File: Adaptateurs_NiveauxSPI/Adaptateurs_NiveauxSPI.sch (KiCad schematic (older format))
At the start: 21 parts, among them P1 CONN_01X07, P2 CONN_01X08, P3 CONN_01X07, P4 CONN_01X12, P5 CONN_01X07, P6 CONN_01X09, P7 CONN_01X07, P8 CONN_01X12, U1 CON_5V_3-3V, U2 CON_5V_3-3V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

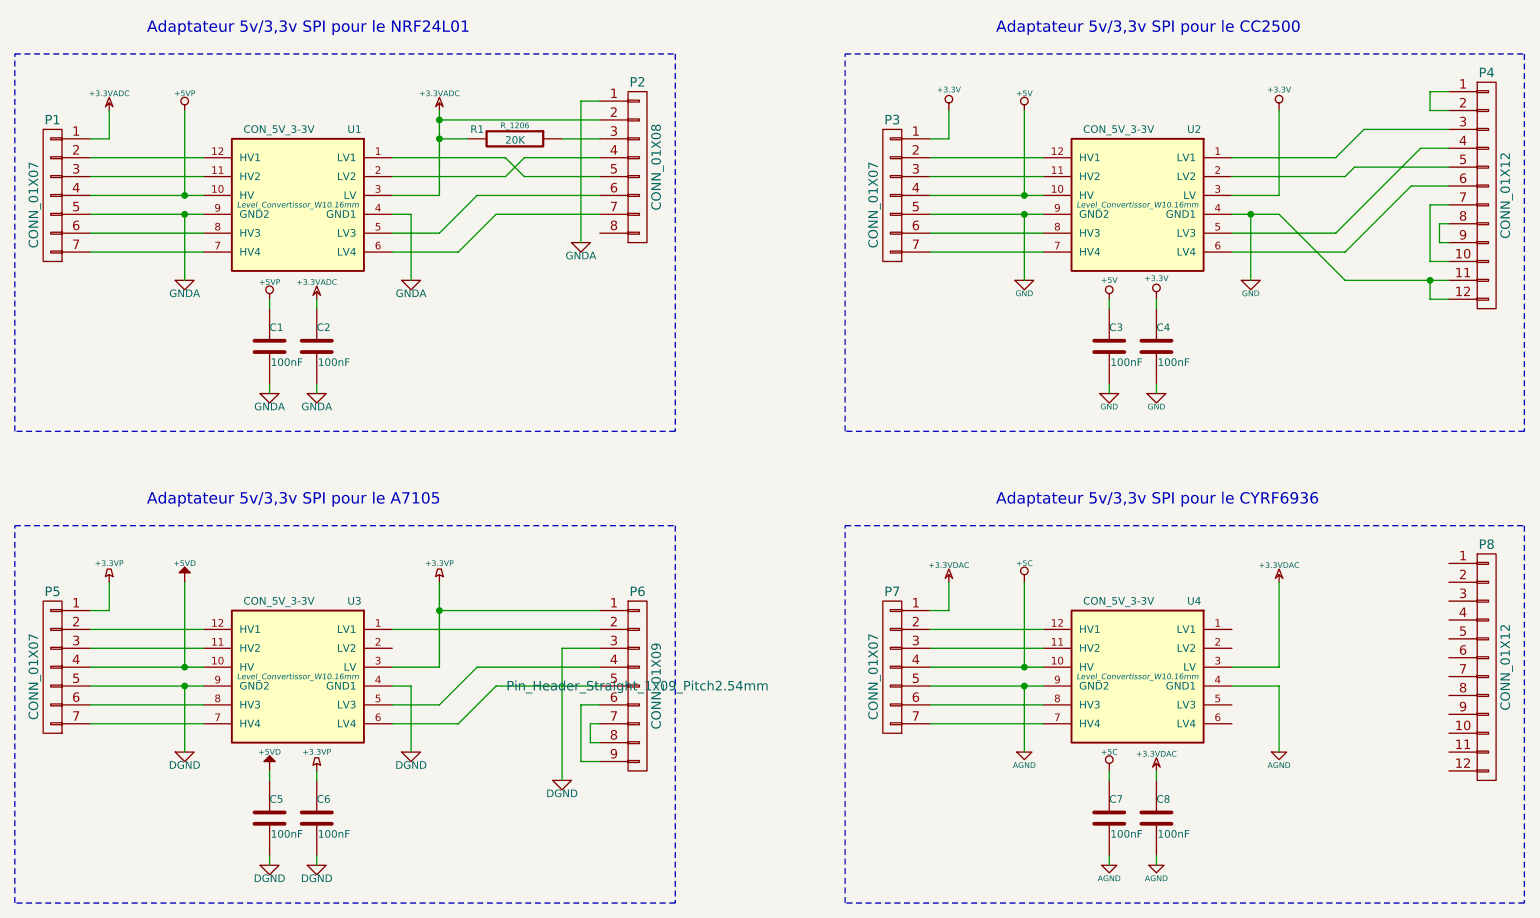
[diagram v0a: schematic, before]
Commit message: Update SPI boards
- Add CYRF9636 board
- Update CC2500 board
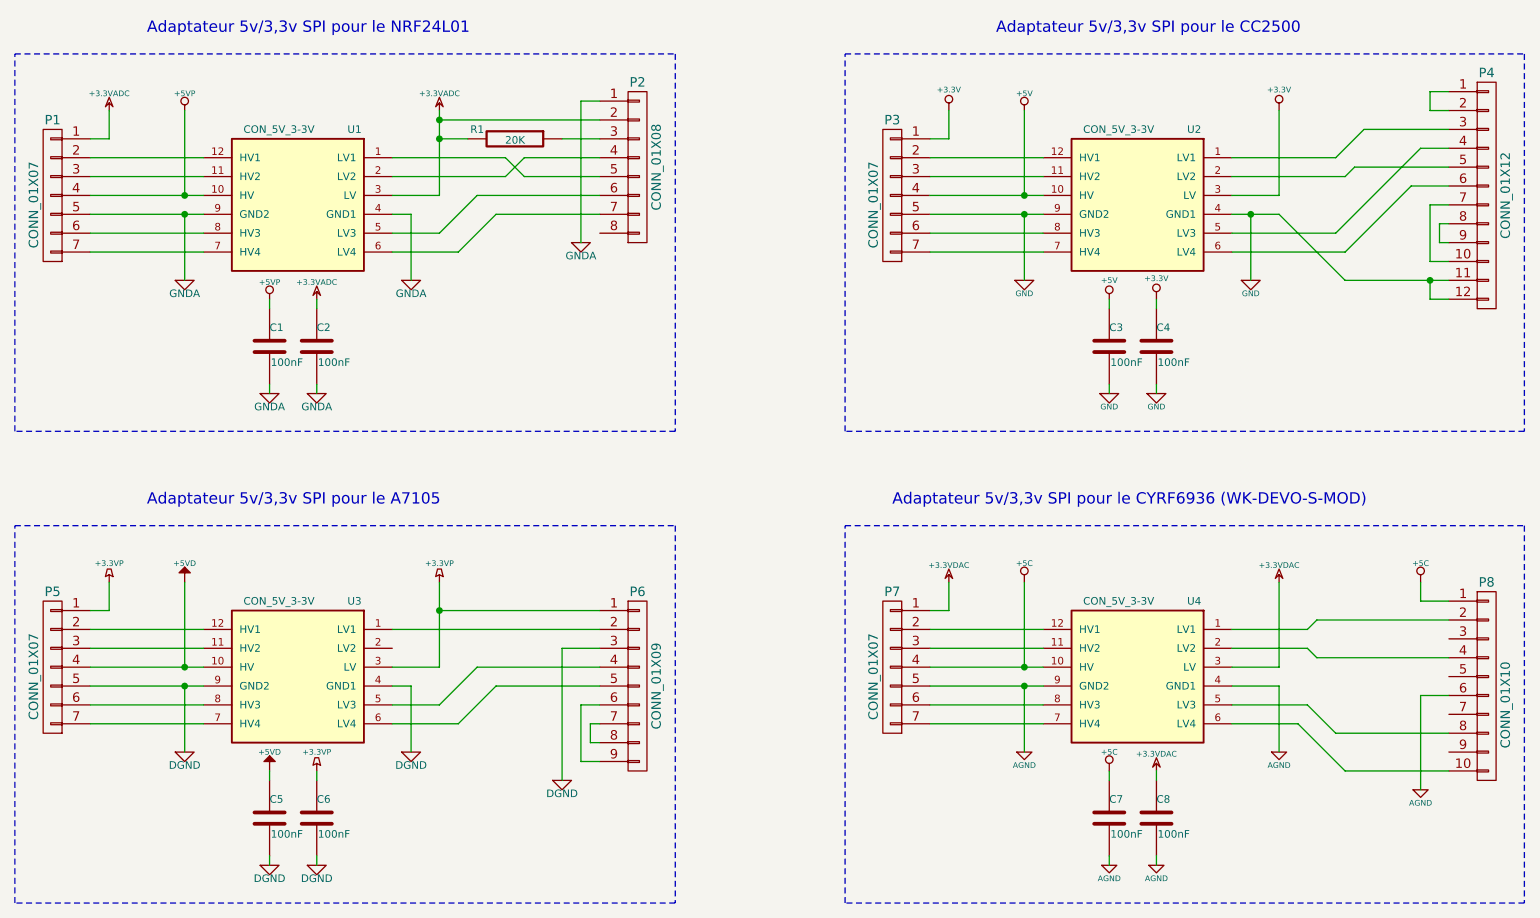
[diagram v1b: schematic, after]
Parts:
- removed P8: CONN_01X12, Pin_Header_Straight_2x06_Pitch2.54mm, symbol CONN_01X12
- added P8: CONN_01X10, Pin_Header_Straight_2x05_Pitch2.54mm, symbol CONN_01X10
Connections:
- net +5C: now also P8.1 (P1)
- net AGND: now also P8.6 (P6)
- net at U4.1 (LV1): now also P8.2 (P2)
- net at U4.2 (LV2): now also P8.4 (P4)
- net at U4.5 (LV3): now also P8.8 (P8)
- net at U4.6 (LV4): now also P8.10 (P10)
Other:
- note added: "Adaptateur 5v/3,3v SPI pour le CYRF6936 (WK-DEVO-S-MOD)"
- note removed: "Adaptateur 5v/3,3v SPI pour le CYRF6936"
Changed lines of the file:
@@
 Sheet 1 1
 Title "Adaptateur Niveaux SPI 5v/3,3v"
-Date "2018-08-24"
+Date "2018-09-07"
 Rev "0.1"
 Comp ""
@@
 F 0 "U1" H 2900 3000 40  0000 C CNN
 F 1 "CON_5V_3-3V" H 3300 3000 40  0000 C CNN
-F 2 "Level_Convertissor_W10.16mm" H 3200 2600 30  0000 C CIN
+F 2 "Level_Convertissor_W10.16mm" H 3200 2600 30  0001 C CIN
 F 3 "" H 3200 2600 60  0001 C CNN
 	1    3200 2600
@@
 F 0 "R1" V 4300 2050 40  0000 C CNN
 F 1 "20K" V 4357 2251 40  0000 C CNN
-F 2 "R_1206" V 4280 2250 30  0000 C CNN
+F 2 "R_1206" V 4280 2250 30  0001 C CNN
 F 3 "" H 4350 2250 30  0000 C CNN
 	1    4350 2250
@@
 F 0 "U2" H 7350 3000 40  0000 C CNN
 F 1 "CON_5V_3-3V" H 7750 3000 40  0000 C CNN
-F 2 "Level_Convertissor_W10.16mm" H 7650 2600 30  0000 C CIN
+F 2 "Level_Convertissor_W10.16mm" H 7650 2600 30  0001 C CIN
 F 3 "" H 7650 2600 60  0001 C CNN
 	1    7650 2600
@@
 F 0 "U3" H 2900 5500 40  0000 C CNN
 F 1 "CON_5V_3-3V" H 3300 5500 40  0000 C CNN
-F 2 "Level_Convertissor_W10.16mm" H 3200 5100 30  0000 C CIN
+F 2 "Level_Convertissor_W10.16mm" H 3200 5100 30  0001 C CIN
 F 3 "" H 3200 5100 60  0001 C CNN
 	1    3200 5100
@@
 F 0 "P6" H 5000 5650 50  0000 C CNN
 F 1 "CONN_01X09" V 5100 5150 50  0000 C CNN
-F 2 "Pin_Header_Straight_1x09_Pitch2.54mm" H 5000 5150 50  0000 C CNN
+F 2 "Pin_Header_Straight_1x09_Pitch2.54mm" H 5000 5150 50  0001 C CNN
 F 3 "" H 5000 5150 50  0000 C CNN
 	1    5000 5150
@@
 Wire Wire Line
 	4700 5250 4800 5250
-$Comp
-L CONN_01X12 P8
-U 1 1 5B812A01
-P 9450 5050
-F 0 "P8" H 9500 5700 50  0000 C CNN
-F 1 "CONN_01X12" V 9600 5050 50  0000 C CNN
-F 2 "Pin_Header_Straight_2x06_Pitch2.54mm" H 9500 4850 50  0001 C CNN
-F 3 "" H 9500 4850 50  0000 C CNN
-	1    9450 5050
-	1    0    0    -1
-$EndComp
 $Comp
 L CONN_01X07 P7
@@
 F 0 "U4" H 7350 5500 40  0000 C CNN
 F 1 "CON_5V_3-3V" H 7750 5500 40  0000 C CNN
-F 2 "Level_Convertissor_W10.16mm" H 7650 5100 30  0000 C CIN
+F 2 "Level_Convertissor_W10.16mm" H 7650 5100 30  0001 C CIN
 F 3 "" H 7650 5100 60  0001 C CNN
 	1    7650 5100
@@
 	6650 4750 6550 4750
 Connection ~ 7050 5050
-Text Notes 6900 4200 0    60   ~ 0
-Adaptateur 5v/3,3v SPI pour le CYRF6936
+Text Notes 6350 4200 0    60   ~ 0
+Adaptateur 5v/3,3v SPI pour le CYRF6936 (WK-DEVO-S-MOD)
 $Comp
 L C C8
@@
 	1    0    0    -1
 $EndComp
+$Comp
+L CONN_01X10 P8
+U 1 1 5B92420B
+P 9450 5250
+F 0 "P8" H 9500 5900 50  0000 C CNN
+F 1 "CONN_01X10" V 9600 5250 50  0000 C CNN
+F 2 "Pin_Header_Straight_2x05_Pitch2.54mm" H 9500 5050 50  0001 C CNN
+F 3 "" H 9500 5050 50  0000 C CNN
+	1    9450 5250
+	1    0    0    -1
+$EndComp
+Wire Wire Line
+	9300 4700 9150 4700
+Wire Wire Line
+	9150 4700 9150 4600
+$Comp
+L +5C #PWR39
+U 1 1 5B9244FF
+P 9150 4600
+F 0 "#PWR39" H 9150 4550 20  0001 C CNN
+F 1 "+5C" H 9150 4700 30  0000 C CNN
+F 2 "" H 9150 4600 60  0001 C CNN
+F 3 "" H 9150 4600 60  0001 C CNN
+	1    9150 4600
+	1    0    0    -1
+$EndComp
+Wire Wire Line
+	9300 5200 9150 5200
+Wire Wire Line
+	9150 5200 9150 5700
+$Comp
+L AGND #PWR40
+U 1 1 5B924863
+P 9150 5700
+F 0 "#PWR40" H 9150 5700 40  0001 C CNN
+F 1 "AGND" H 9150 5630 30  0000 C CNN
+F 2 "" H 9150 5700 60  0001 C CNN
+F 3 "" H 9150 5700 60  0001 C CNN
+	1    9150 5700
+	1    0    0    -1
+$EndComp
+Wire Wire Line
+	8150 4850 8550 4850
+Wire Wire Line
+	8550 4850 8600 4800
+Wire Wire Line
+	8600 4800 9300 4800
+Wire Wire Line
+	8150 4950 8550 4950
+Wire Wire Line
+	8550 4950 8600 5000
+Wire Wire Line
+	8600 5000 9300 5000
+Wire Wire Line
+	8150 5250 8550 5250
+Wire Wire Line
+	8550 5250 8700 5400
+Wire Wire Line
+	8700 5400 9300 5400
+Wire Wire Line
+	8150 5350 8500 5350
+Wire Wire Line
+	8500 5350 8750 5600
+Wire Wire Line
+	8750 5600 9300 5600
 $EndSCHEMATC
